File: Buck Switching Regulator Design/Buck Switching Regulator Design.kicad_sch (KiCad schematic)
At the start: 12 parts, among them U1 MP2322GQH-P

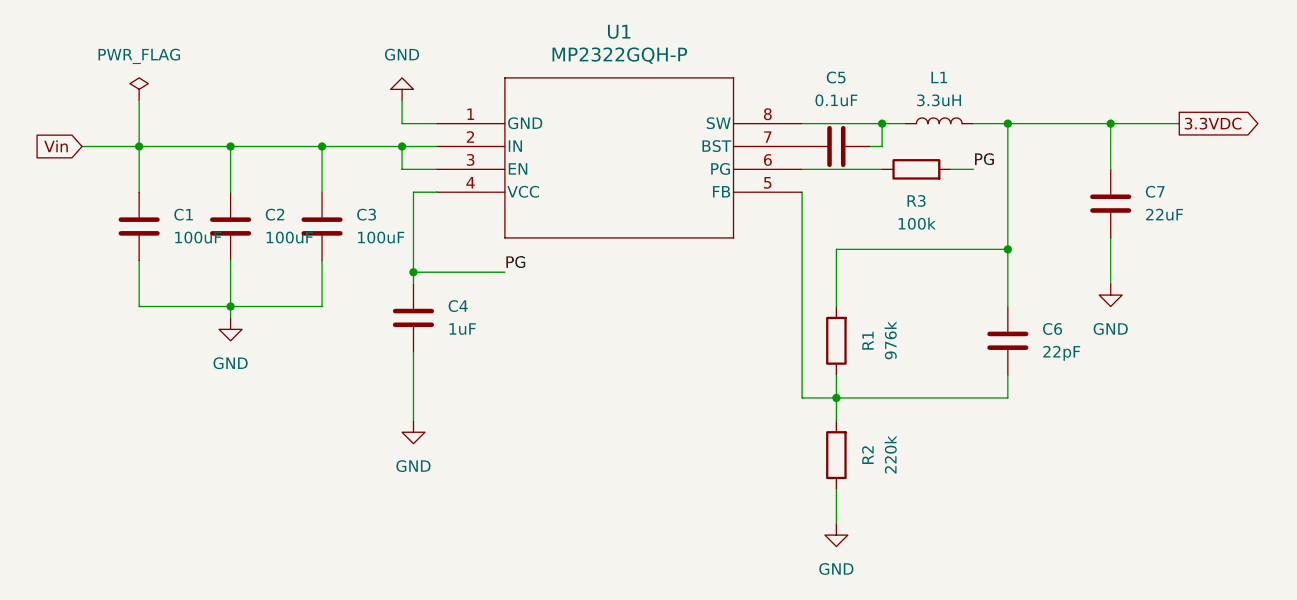
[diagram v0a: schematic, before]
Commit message: Updated Footprints
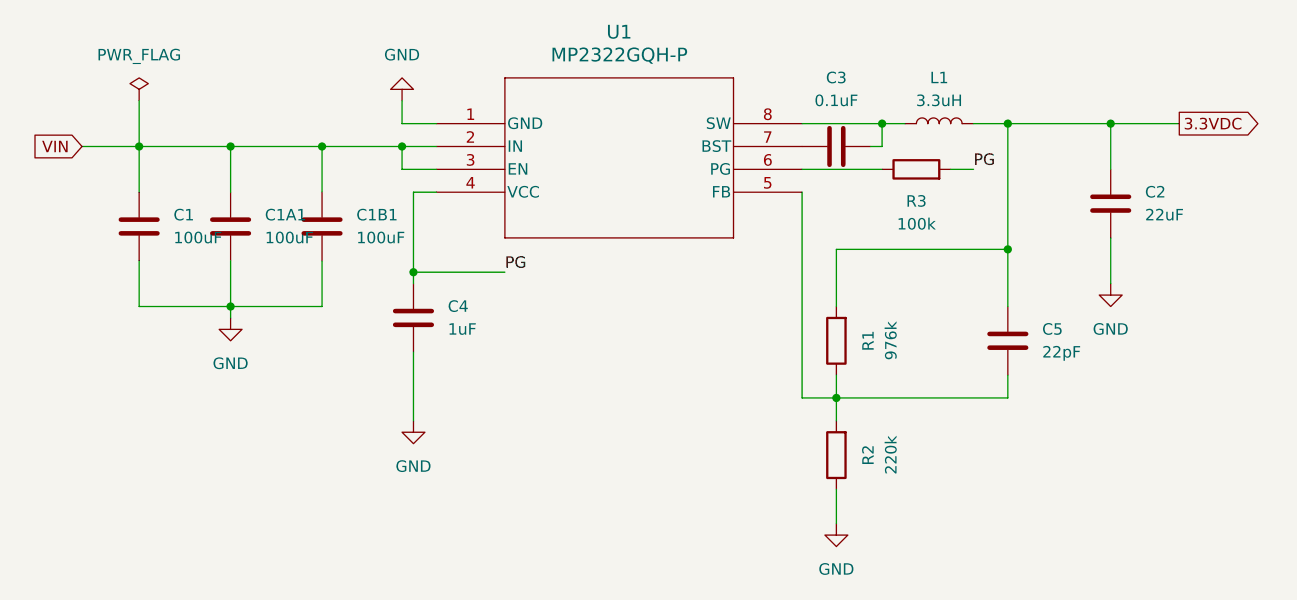
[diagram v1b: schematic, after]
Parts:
- C1: footprint (none) -> Capacitor_SMD:C_1210_3225Metric
- C1A1: renamed from C2; footprint (none) -> Capacitor_SMD:C_1210_3225Metric
- C1B1: renamed from C3; footprint (none) -> Capacitor_SMD:C_1210_3225Metric
- C2: renamed from C7; footprint (none) -> Capacitor_SMD:C_1206_3216Metric
- C3: renamed from C5; footprint (none) -> Capacitor_SMD:C_0603_1608Metric
- C4: footprint (none) -> Capacitor_SMD:C_0603_1608Metric
- C5: renamed from C6; footprint (none) -> Capacitor_SMD:C_0603_1608Metric
- L1: footprint (none) -> Inductor_SMD:L_7.3x7.3_H3.5
- R1, R2, R3: footprint (none) -> Resistor_SMD:R_0603_1608Metric
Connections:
- net Vin renamed VIN
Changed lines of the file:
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@@
 		)
 	)
-	(global_label "Vin"
+	(global_label "VIN"
 		(shape input)
 		(at 81.28 96.52 180)
@@
 		)
 		(property "Intersheetrefs" "${INTERSHEET_REFS}"
-			(at 75.4524 96.52 0)
+			(at 75.2709 96.52 0)
 			(effects
 				(font
@@
 		(dnp no)
 		(fields_autoplaced yes)
-		(property "Reference" "C3"
+		(property "Reference" "C1B1"
 			(at 111.76 104.1399 0)
 			(effects
@@
 			)
 		)
-		(property "Footprint" ""
+		(property "Footprint" "Capacitor_SMD:C_1210_3225Metric"
 			(at 108.9152 109.22 0)
 			(effects
@@
 			(project ""
 				(path "/e947e11b-5739-405f-8d66-ab11be7e6c26"
-					(reference "C3")
+					(reference "C1B1")
 					(unit 1)
 				)
@@
 			)
 		)
-		(property "Footprint" ""
+		(property "Footprint" "Resistor_SMD:R_0603_1608Metric"
 			(at 173.99 100.838 90)
 			(effects
@@
 			)
 		)
-		(property "Footprint" ""
+		(property "Footprint" "Resistor_SMD:R_0603_1608Metric"
 			(at 166.878 130.81 90)
 			(effects
@@
 		(on_board yes)
 		(dnp no)
-		(property "Reference" "C6"
+		(property "Reference" "C5"
 			(at 187.96 116.8399 0)
 			(effects
@@
 			)
 		)
-		(property "Footprint" ""
+		(property "Footprint" "Capacitor_SMD:C_0603_1608Metric"
 			(at 183.1848 114.3 0)
 			(effects
@@
 			(project "Buck Switching Regulator Design"
 				(path "/e947e11b-5739-405f-8d66-ab11be7e6c26"
-					(reference "C6")
+					(reference "C5")
 					(unit 1)
 				)
@@
 			)
 		)
-		(property "Footprint" ""
+		(property "Footprint" "Capacitor_SMD:C_0603_1608Metric"
 			(at 119.0752 119.38 0)
 			(effects
@@
 			)
 		)
-		(property "Footprint" ""
+		(property "Footprint" "Inductor_SMD:L_7.3x7.3_H3.5"
 			(at 176.53 93.98 0)
 			(effects
@@
 		(dnp no)
 		(fields_autoplaced yes)
-		(property "Reference" "C7"
+		(property "Reference" "C2"
 			(at 199.39 101.5999 0)
 			(effects
@@
 			)
 		)
-		(property "Footprint" ""
+		(property "Footprint" "Capacitor_SMD:C_1206_3216Metric"
 			(at 194.6148 99.06 0)
 			(effects
@@
 			(project "Buck Switching Regulator Design"
 				(path "/e947e11b-5739-405f-8d66-ab11be7e6c26"
-					(reference "C7")
+					(reference "C2")
 					(unit 1)
 				)
@@
 		(dnp no)
 		(fields_autoplaced yes)
-		(property "Reference" "C5"
+		(property "Reference" "C3"
 			(at 165.1 88.9 90)
 			(effects
@@
 			)
 		)
-		(property "Footprint" ""
+		(property "Footprint" "Capacitor_SMD:C_0603_1608Metric"
 			(at 168.91 95.5548 0)
 			(effects
@@
 			(project "Buck Switching Regulator Design"
 				(path "/e947e11b-5739-405f-8d66-ab11be7e6c26"
-					(reference "C5")
+					(reference "C3")
+					(unit 1)
+				)
+			)
+		)
+	)
+	(symbol
+		(lib_id "Switching_Regulator_Design:MP2322GQH-P")
+		(at 120.65 93.98 0)
+		(unit 1)
+		(exclude_from_sim no)
+		(in_bom yes)
+		(on_board yes)
+		(dnp no)
+		(fields_autoplaced yes)
+		(property "Reference" "U1"
+			(at 140.97 83.82 0)
+			(effects
+				(font
+					(size 1.524 1.524)
+				)
+			)
+		)
+		(property "Value" "MP2322GQH-P"
+			(at 140.97 86.36 0)
+			(effects
+				(font
+					(size 1.524 1.524)
+				)
+			)
+		)
+		(property "Footprint" "Switching_Regulator_Design:QFN-8_1p5MMx2MM_MNP"
+			(at 120.65 93.98 0)
+			(effects
+				(font
+					(size 1.27 1.27)
+					(italic yes)
+				)
+				(hide yes)
+			)
+		)
+		(property "Datasheet" "https://www.monolithicpower.com/en/documentview/productdocument/index/version/2/document_type/Datasheet/lang/en/sku/MP2322"
+			(at 120.65 93.98 0)
+			(effects
+				(font
+					(size 1.27 1.27)
+					(italic yes)
+				)
+				(hide yes)
+			)
+		)
+		(property "Description" ""
+			(at 120.65 93.98 0)
+			(effects
+				(font
+					(size 1.27 1.27)
+				)
+				(hide yes)
+			)
+		)
+		(pin "6"
+		)
+		(pin "7"
+		)
+		(pin "5"
+		)
+		(pin "4"
+		)
+		(pin "1"
+		)
+		(pin "2"
+		)
+		(pin "3"
+		)
+		(pin "8"
+		)
+		(instances
+			(project ""
+				(path "/e947e11b-5739-405f-8d66-ab11be7e6c26"
+					(reference "U1")
 					(unit 1)
 				)
@@
 			)
 		)
-		(property "Footprint" ""
+		(property "Footprint" "Capacitor_SMD:C_1210_3225Metric"
 			(at 88.5952 109.22 0)
 			(effects
@@
 		(dnp no)
 		(fields_autoplaced yes)
-		(property "Reference" "C2"
+		(property "Reference" "C1A1"
 			(at 101.6 104.1399 0)
 			(effects
@@
 			)
 		)
-		(property "Footprint" ""
+		(property "Footprint" "Capacitor_SMD:C_1210_3225Metric"
 			(at 98.7552 109.22 0)
 			(effects
@@
 			(project ""
 				(path "/e947e11b-5739-405f-8d66-ab11be7e6c26"
-					(reference "C2")
-					(unit 1)
-				)
-			)
-		)
-	)
-	(symbol
-		(lib_id "Switching_Regulator_Design:MP2322GQH-P")
-		(at 120.65 93.98 0)
-		(unit 1)
-		(exclude_from_sim no)
-		(in_bom yes)
-		(on_board yes)
-		(dnp no)
-		(fields_autoplaced yes)
-		(property "Reference" "U1"
-			(at 140.97 83.82 0)
-			(effects
-				(font
-					(size 1.524 1.524)
-				)
-			)
-		)
-		(property "Value" "MP2322GQH-P"
-			(at 140.97 86.36 0)
-			(effects
-				(font
-					(size 1.524 1.524)
-				)
-			)
-		)
-		(property "Footprint" "Switching_Regulator_Design:QFN-8_1p5MMx2MM_MNP"
-			(at 120.65 93.98 0)
-			(effects
-				(font
-					(size 1.27 1.27)
-					(italic yes)
-				)
-				(hide yes)
-			)
-		)
-		(property "Datasheet" "https://www.monolithicpower.com/en/documentview/productdocument/index/version/2/document_type/Datasheet/lang/en/sku/MP2322"
-			(at 120.65 93.98 0)
-			(effects
-				(font
-					(size 1.27 1.27)
-					(italic yes)
-				)
-				(hide yes)
-			)
-		)
-		(property "Description" ""
-			(at 120.65 93.98 0)
-			(effects
-				(font
-					(size 1.27 1.27)
-				)
-				(hide yes)
-			)
-		)
-		(pin "6"
-		)
-		(pin "5"
-		)
-		(pin "4"
-		)
-		(pin "1"
-		)
-		(pin "7"
-		)
-		(pin "8"
-		)
-		(pin "2"
-		)
-		(pin "3"
-		)
-		(instances
-			(project ""
-				(path "/e947e11b-5739-405f-8d66-ab11be7e6c26"
-					(reference "U1")
+					(reference "C1A1")
 					(unit 1)
 				)
@@
 			)
 		)
-		(property "Footprint" ""
+		(property "Footprint" "Resistor_SMD:R_0603_1608Metric"
 			(at 166.878 118.11 90)
 			(effects

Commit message: PCB Layout: Components Placed
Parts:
- C1, C1A1, C1B1: footprint Capacitor_SMD:C_1210_3225Metric -> Capacitor_SMD:C_0603_1608Metric
- L1: footprint Inductor_SMD:L_7.3x7.3_H3.5 -> Inductor_SMD:L_Walsin_WLFM252009x
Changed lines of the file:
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@@
 			)
 		)
-		(property "Footprint" "Capacitor_SMD:C_1210_3225Metric"
+		(property "Footprint" "Capacitor_SMD:C_0603_1608Metric"
 			(at 108.9152 109.22 0)
 			(effects
@@
 			)
 		)
-		(property "Footprint" "Inductor_SMD:L_7.3x7.3_H3.5"
+		(property "Footprint" "Inductor_SMD:L_Walsin_WLFM252009x"
 			(at 176.53 93.98 0)
 			(effects
@@
 			)
 		)
-		(property "Footprint" "Capacitor_SMD:C_1210_3225Metric"
+		(property "Footprint" "Capacitor_SMD:C_0603_1608Metric"
 			(at 88.5952 109.22 0)
 			(effects
@@
 			)
 		)
-		(property "Footprint" "Capacitor_SMD:C_1210_3225Metric"
+		(property "Footprint" "Capacitor_SMD:C_0603_1608Metric"
 			(at 98.7552 109.22 0)
 			(effects
